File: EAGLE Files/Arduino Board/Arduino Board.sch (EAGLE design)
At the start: 12 parts

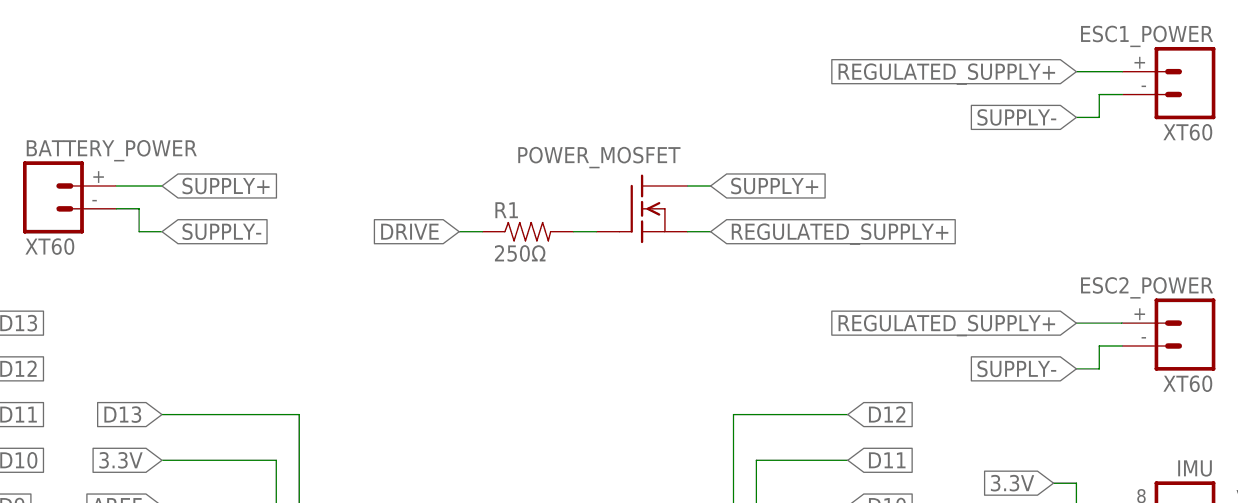
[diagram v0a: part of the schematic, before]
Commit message: Corrected schematic error where MOSFET was wired incorrectly in circuit
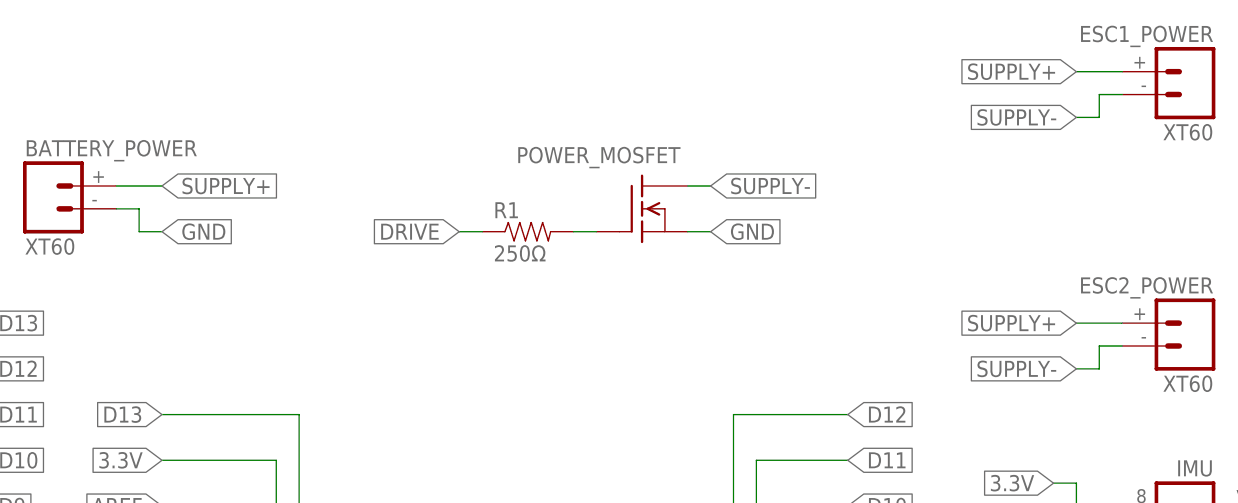
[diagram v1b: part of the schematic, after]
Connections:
- removed net REGULATED_SUPPLY+: ESC1_POWER.2, ESC2_POWER.2, POWER_MOSFET.S
- net GND: now also BATTERY_POWER.1, POWER_MOSFET.S
- net SUPPLY+: now also ESC1_POWER.2, ESC2_POWER.2; no longer POWER_MOSFET.D
- net SUPPLY-: now also POWER_MOSFET.D; no longer BATTERY_POWER.1
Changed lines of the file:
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@@
 <label x="-53.34" y="-45.72" size="1.778" layer="95" xref="yes"/>
+</segment>
+<segment>
+<pinref part="POWER_MOSFET" gate="G$1" pin="S"/>
+<wire x1="25.4" y1="81.28" x2="27.94" y2="81.28" width="0.1524" layer="91"/>
+<label x="27.94" y="81.28" size="1.778" layer="95" xref="yes"/>
+</segment>
+<segment>
+<wire x1="-33.02" y1="81.28" x2="-35.56" y2="81.28" width="0.1524" layer="91"/>
+<wire x1="-35.56" y1="81.28" x2="-35.56" y2="83.82" width="0.1524" layer="91"/>
+<wire x1="-35.56" y1="83.82" x2="-38.1" y2="83.82" width="0.1524" layer="91"/>
+<label x="-33.02" y="81.28" size="1.778" layer="95" xref="yes"/>
+<pinref part="BATTERY_POWER" gate="G$1" pin="1"/>
 </segment>
 </net>
@@
 </segment>
 <segment>
-<pinref part="POWER_MOSFET" gate="G$1" pin="D"/>
-<wire x1="27.94" y1="86.36" x2="25.4" y2="86.36" width="0.1524" layer="91"/>
-<label x="27.94" y="86.36" size="1.778" layer="95" xref="yes"/>
-</segment>
-</net>
-<net name="REGULATED_SUPPLY+" class="0">
-<segment>
-<pinref part="POWER_MOSFET" gate="G$1" pin="S"/>
-<wire x1="25.4" y1="81.28" x2="27.94" y2="81.28" width="0.1524" layer="91"/>
-<label x="27.94" y="81.28" size="1.778" layer="95" xref="yes"/>
-</segment>
-<segment>
 <wire x1="68.58" y1="99.06" x2="73.66" y2="99.06" width="0.1524" layer="91"/>
 <label x="68.58" y="99.06" size="1.778" layer="95" rot="R180" xref="yes"/>
@@
 </segment>
 <segment>
-<wire x1="-33.02" y1="81.28" x2="-35.56" y2="81.28" width="0.1524" layer="91"/>
-<wire x1="-35.56" y1="81.28" x2="-35.56" y2="83.82" width="0.1524" layer="91"/>
-<wire x1="-35.56" y1="83.82" x2="-38.1" y2="83.82" width="0.1524" layer="91"/>
-<label x="-33.02" y="81.28" size="1.778" layer="95" xref="yes"/>
-<pinref part="BATTERY_POWER" gate="G$1" pin="1"/>
-</segment>
-<segment>
 <wire x1="73.66" y1="68.58" x2="71.12" y2="68.58" width="0.1524" layer="91"/>
 <wire x1="71.12" y1="68.58" x2="71.12" y2="66.04" width="0.1524" layer="91"/>
@@
 <pinref part="ESC2_POWER" gate="G$1" pin="1"/>
 </segment>
+<segment>
+<pinref part="POWER_MOSFET" gate="G$1" pin="D"/>
+<wire x1="27.94" y1="86.36" x2="25.4" y2="86.36" width="0.1524" layer="91"/>
+<label x="27.94" y="86.36" size="1.778" layer="95" xref="yes"/>
+</segment>
 </net>

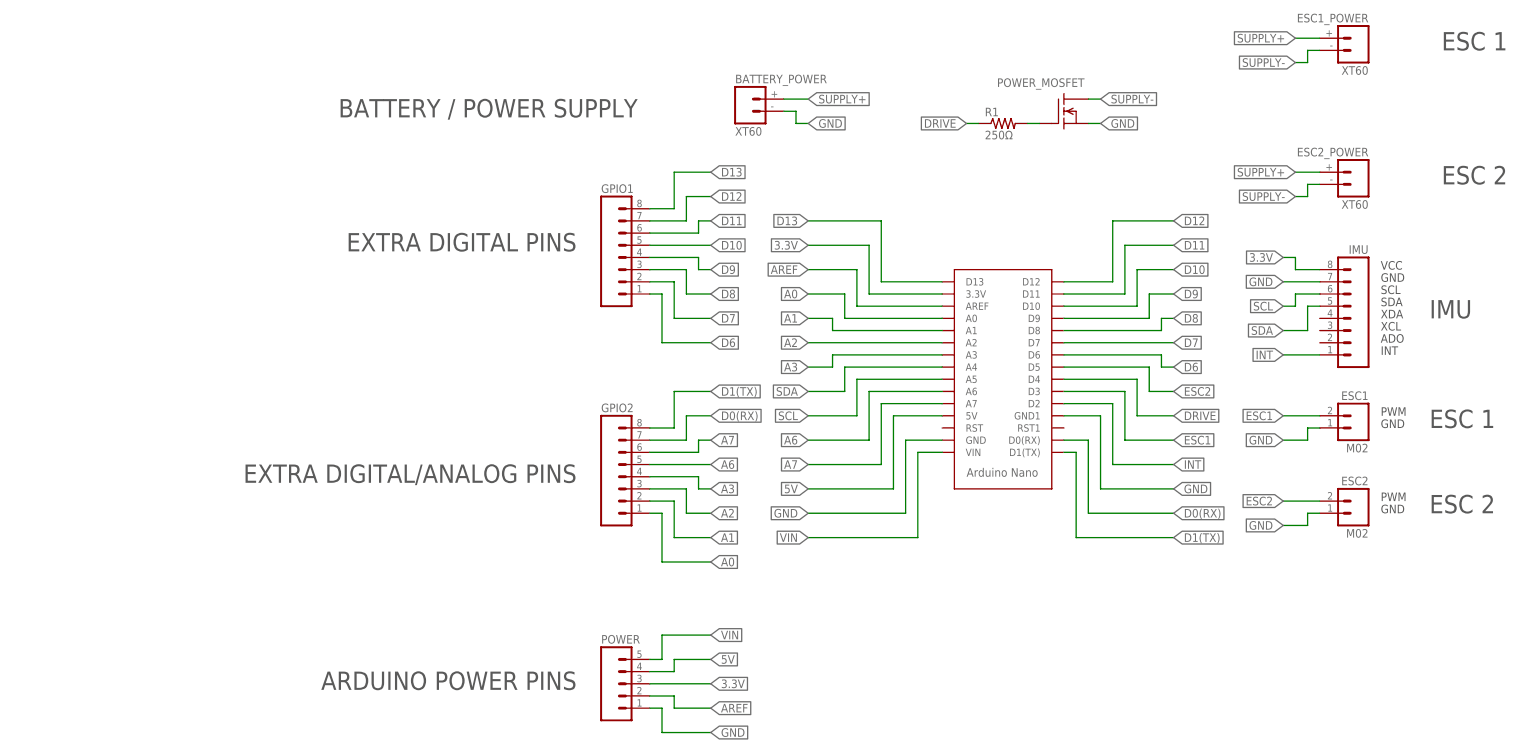
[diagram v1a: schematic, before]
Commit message: Added voltage divider for simple battery monitoring
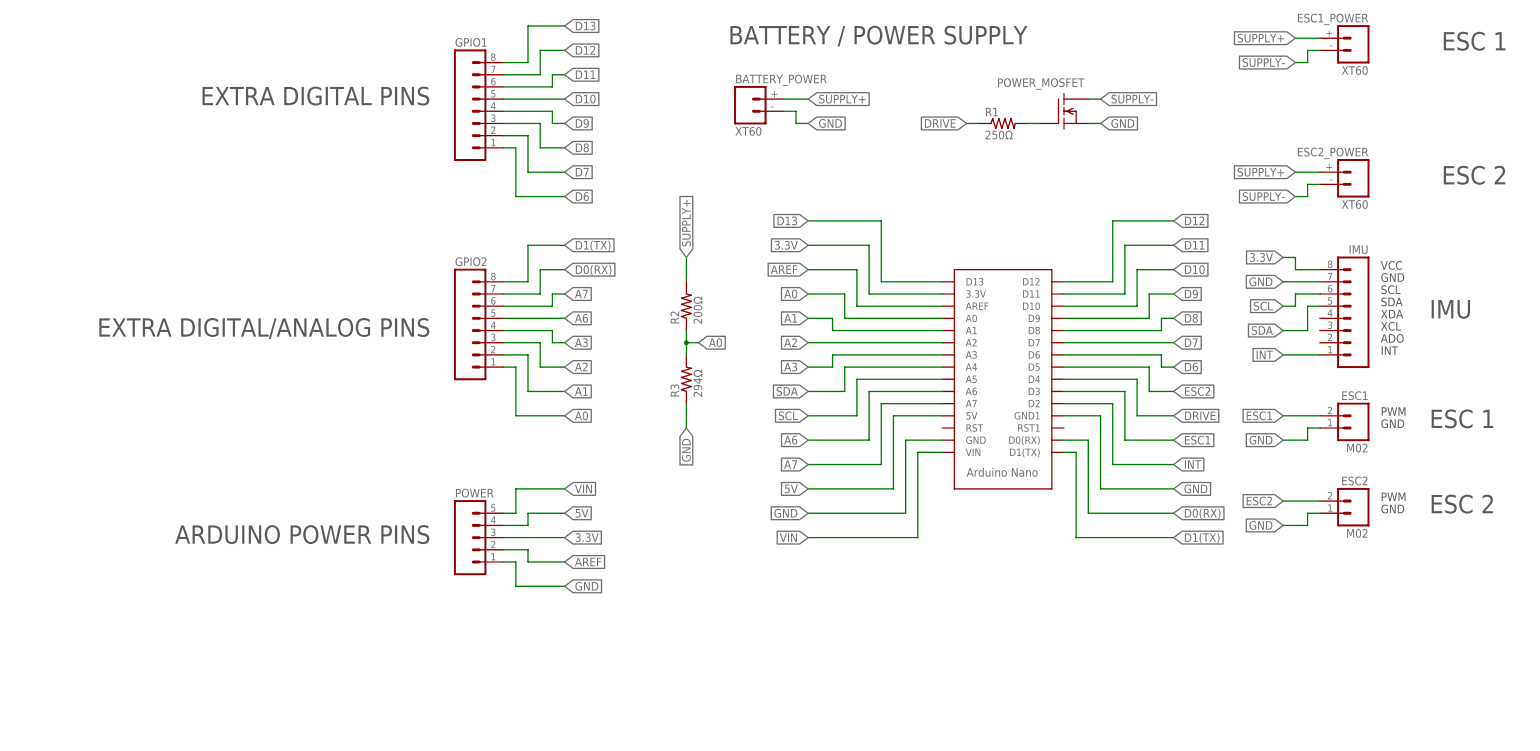
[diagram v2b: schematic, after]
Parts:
- added R2: 200Ω, Controls Library:RESISTORPTH-1/4W
- added R3: 294Ω, Controls Library:RESISTORPTH-1/4W
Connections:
- net A0: now also R2.1, R3.2
- net GND: now also R3.1
- net SUPPLY+: now also R2.2
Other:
- moved on the sheet: GPIO1, GPIO2, POWER

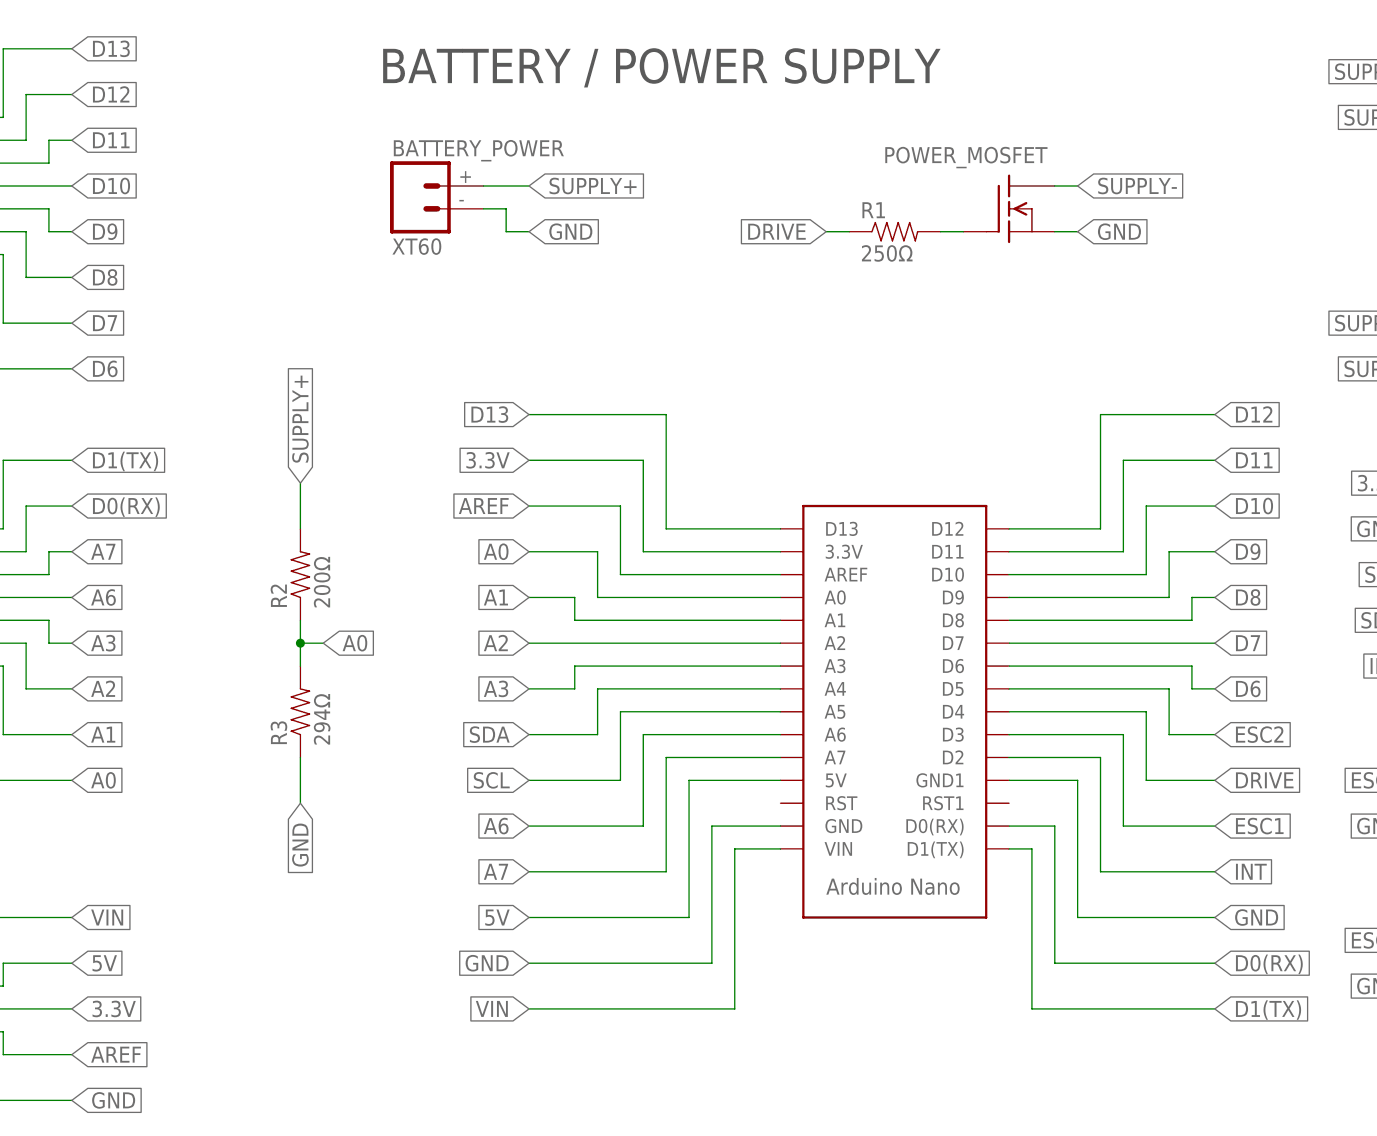
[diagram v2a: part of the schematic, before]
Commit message: Small changes to PCB design files from EAGLE software update
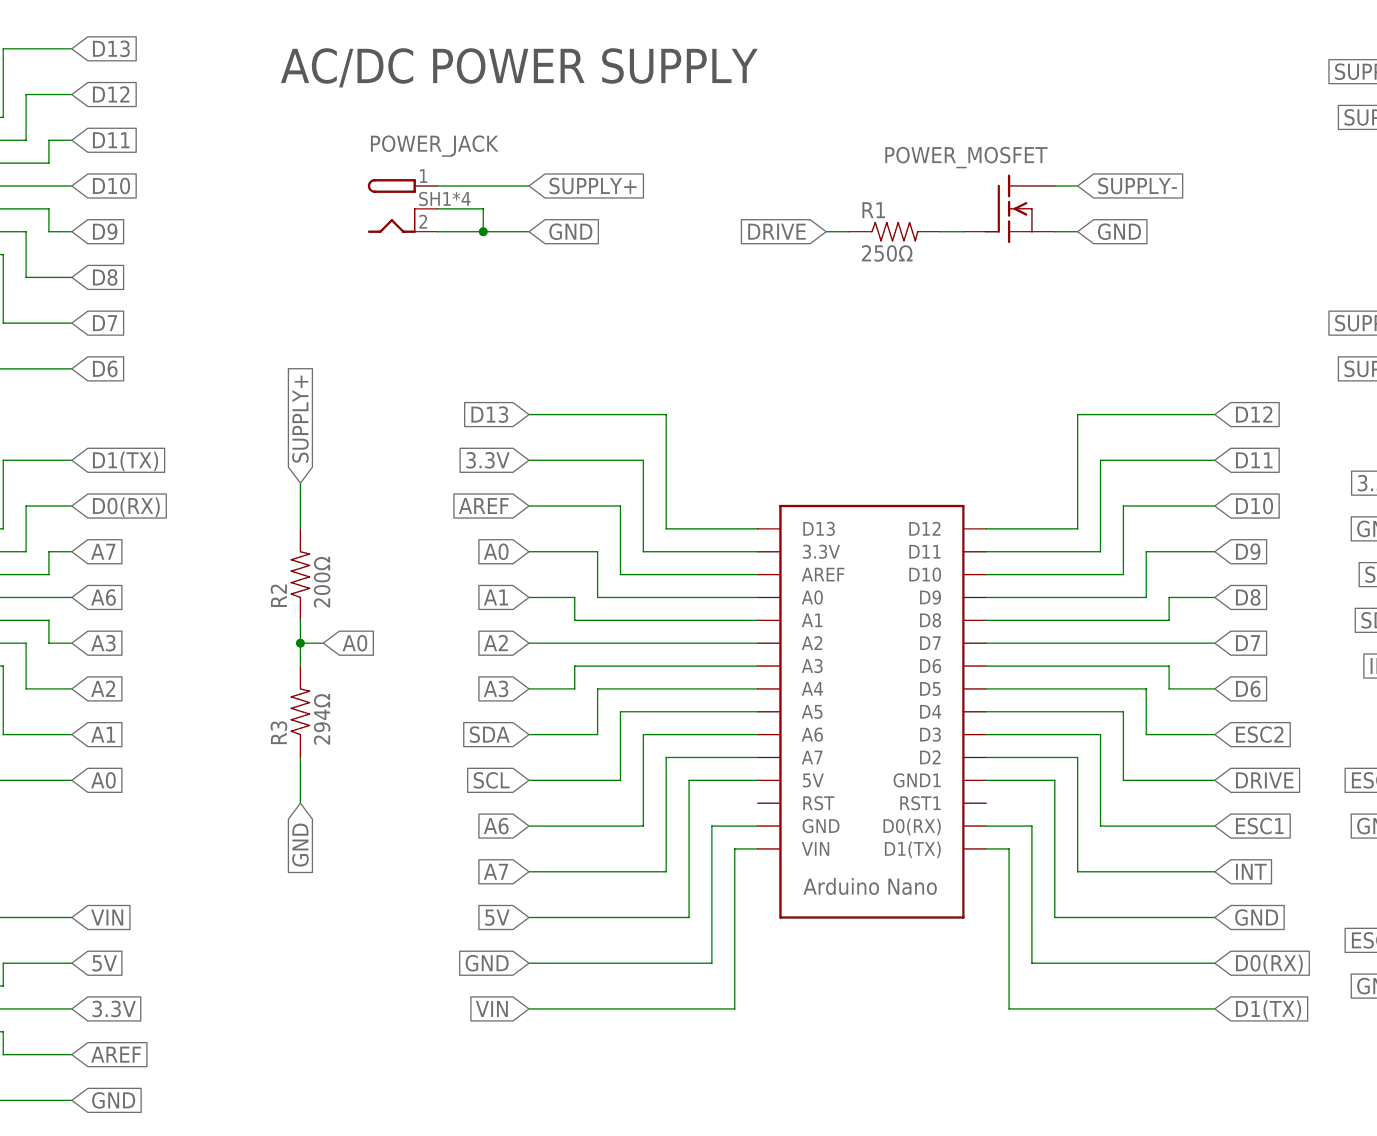
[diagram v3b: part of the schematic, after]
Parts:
- removed BATTERY_POWER: XT60, Controls Library:XT60
- added POWER_JACK: PJ-082BH, Controls Library:PJ-082BH
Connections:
- net GND: now also POWER_JACK.GND, POWER_JACK.SHIELD; no longer BATTERY_POWER.1
- net SUPPLY+: now also POWER_JACK.PWR; no longer BATTERY_POWER.2
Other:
- note added: "AC/DC POWER SUPPLY"
- note removed: "BATTERY / POWER SUPPLY"
